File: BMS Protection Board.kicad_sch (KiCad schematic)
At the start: 0 parts

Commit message: worked on MCU
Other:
- sheet BMS_Read_Voltage renamed BMS Read Voltage
- sheet BMS_Thermistors renamed BMS Thermistors
- removed sheet Battery Management System Controller
- added sheet BMS Read Temperature (BMS Read Temperature.kicad_sch)
- sheet BMS Read Voltage: file BMS_Read_Voltage.kicad_sch -> BMS Read Voltage.kicad_sch
- sheet BMS Read Voltage ports: added PACK_READ_STATS; removed PACK_READ_TMP
- sheet BMS Thermistors: file BMS_Thermistors.kicad_sch -> BMS Thermistors.kicad_sch
- sheet Pack Switching and Current Sensing ports: added BATT+, BATT-; removed SCREW_BATT+, SCREW_BATT-

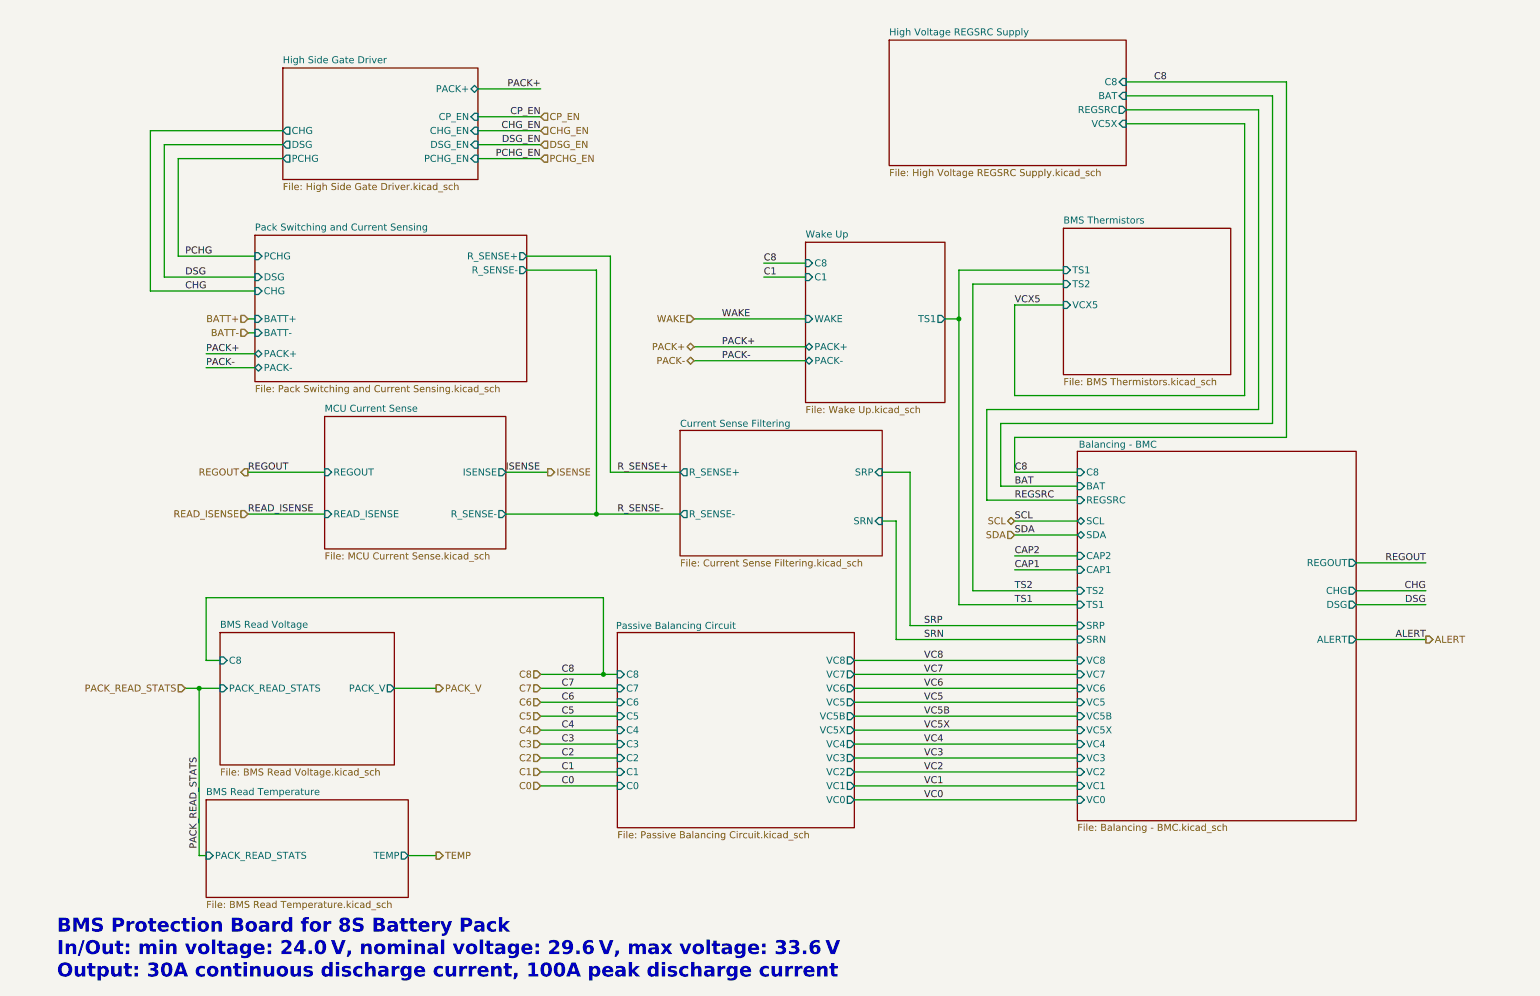
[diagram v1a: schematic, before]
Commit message: commit before simplifying and removing features
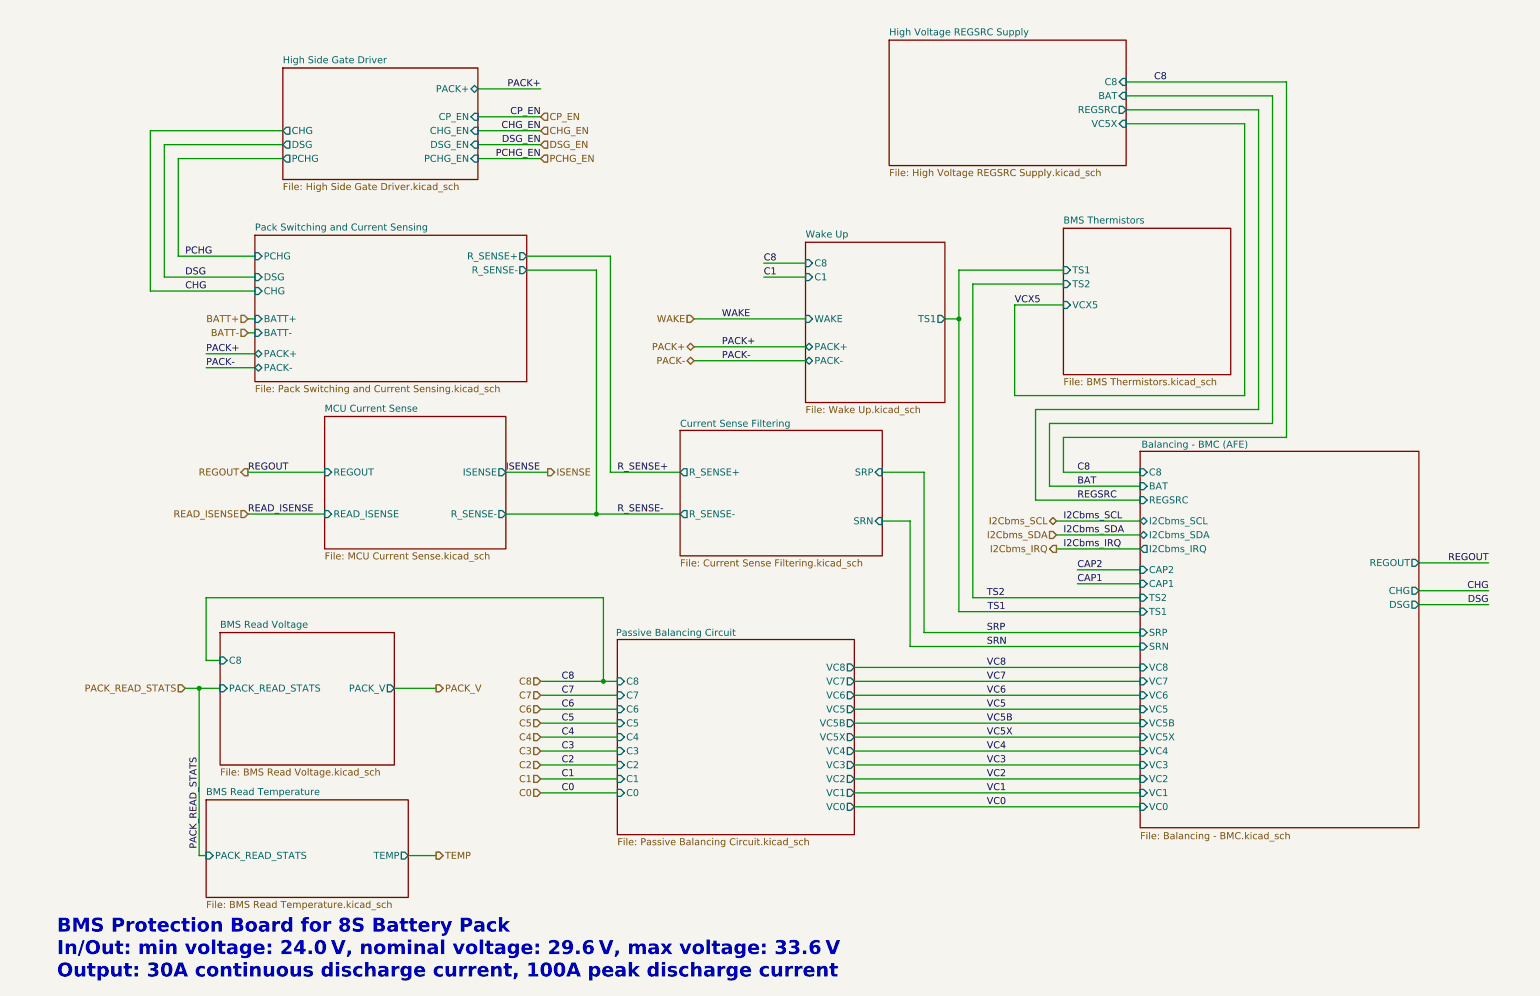
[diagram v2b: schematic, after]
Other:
- sheet Balancing - BMC renamed Balancing - BMC (AFE)
- sheet Balancing - BMC (AFE) ports: added I2Cbms_IRQ, I2Cbms_SCL, I2Cbms_SDA; removed ALERT, SCL, SDA

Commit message: Added Fuel/Gas Guage
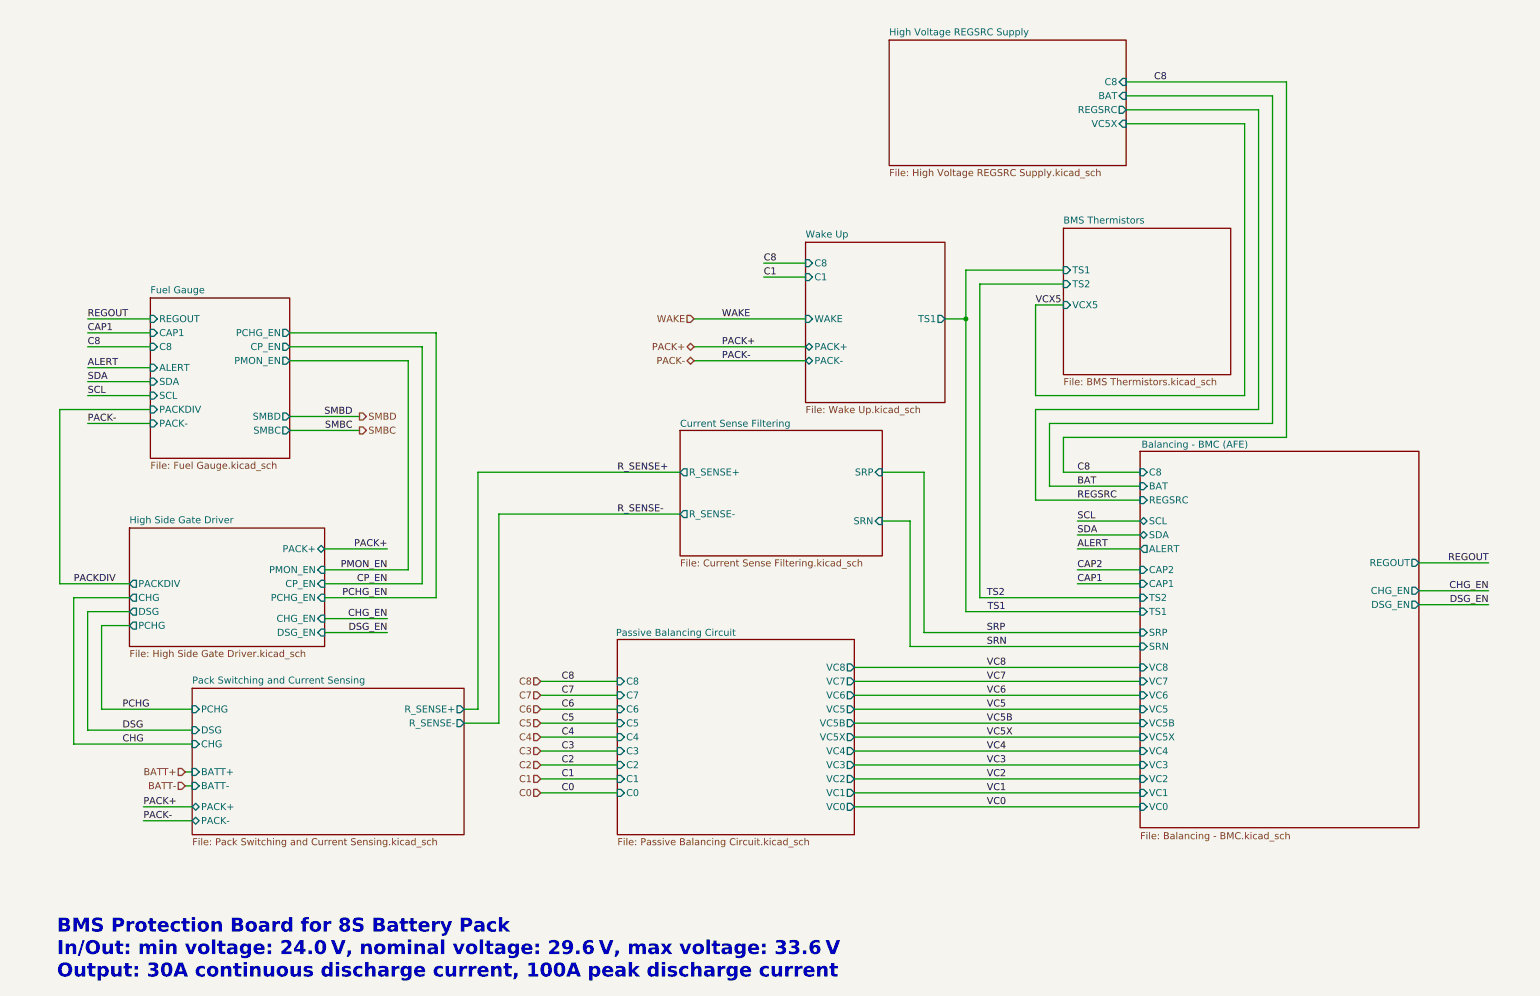
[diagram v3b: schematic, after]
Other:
- removed sheet BMS Read Temperature
- removed sheet BMS Read Voltage
- removed sheet MCU Current Sense
- added sheet Fuel Gauge (Fuel Gauge.kicad_sch)
- sheet Balancing - BMC (AFE) ports: added ALERT, CHG_EN, DSG_EN, SCL, SDA; removed CHG, DSG, I2Cbms_IRQ, I2Cbms_SCL, I2Cbms_SDA
- sheet High Side Gate Driver ports: added PACKDIV, PMON_EN; removed none

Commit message: ready to start first pass review on bms
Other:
- sheet Wake Up ports: added REGOUT; removed C1, PACK-, WAKE
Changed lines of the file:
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@@
-	(wire
-		(pts
-			(xy 138.43 69.85) (xy 158.75 69.85)
-		)
-		(stroke
-			(width 0)
-			(type default)
-		)
-	)
 	(wire
 		(pts
@@
 	(wire
 		(pts
-			(xy 138.43 77.47) (xy 158.75 77.47)
-		)
-		(stroke
-			(width 0)
-			(type default)
-		)
-	)
-	(wire
-		(pts
 			(xy 25.4 120.65) (xy 35.56 120.65)
 		)
@@
 	(wire
 		(pts
-			(xy 151.13 62.23) (xy 158.75 62.23)
+			(xy 158.75 71.12) (xy 146.05 71.12)
 		)
 		(stroke
@@
 	(wire
 		(pts
-			(xy 22.86 118.11) (xy 22.86 86.36)
+			(xy 16.51 118.11) (xy 16.51 86.36)
 		)
 		(stroke
@@
 	(wire
 		(pts
-			(xy 22.86 86.36) (xy 39.37 86.36)
+			(xy 16.51 86.36) (xy 39.37 86.36)
 		)
 		(stroke
@@
 	(wire
 		(pts
-			(xy 22.86 118.11) (xy 35.56 118.11)
+			(xy 16.51 118.11) (xy 35.56 118.11)
 		)
 		(stroke
@@
 		)
 	)
-	(label "WAKE"
-		(at 143.51 69.85 0)
-		(effects
-			(font
-				(size 1.27 1.27)
-			)
-			(justify left bottom)
-		)
-	)
 	(label "DSG_EN"
 		(at 283.21 121.92 180)
@@
 		)
 	)
-	(label "PACK-"
-		(at 143.51 77.47 0)
-		(effects
-			(font
-				(size 1.27 1.27)
-			)
-			(justify left bottom)
-		)
-	)
 	(label "C4"
 		(at 114.3 146.05 0)
@@
 		)
 	)
+	(label "REGOUT"
+		(at 146.05 71.12 0)
+		(effects
+			(font
+				(size 1.27 1.27)
+			)
+			(justify left bottom)
+		)
+	)
 	(label "VC0"
 		(at 191.77 158.75 0)
@@
 	(label "VCX5"
 		(at 200.66 67.31 0)
-		(effects
-			(font
-				(size 1.27 1.27)
-			)
-			(justify left bottom)
-		)
-	)
-	(label "C1"
-		(at 151.13 62.23 0)
 		(effects
 			(font
@@
 		)
 	)
-	(hierarchical_label "PACK-"
-		(shape bidirectional)
-		(at 138.43 77.47 180)
-		(effects
-			(font
-				(size 1.27 1.27)
-			)
-			(justify right)
-		)
-	)
 	(hierarchical_label "C4"
 		(shape input)
@@
 		)
 	)
-	(hierarchical_label "WAKE"
+	(hierarchical_label "PACK-"
 		(shape input)
-		(at 138.43 69.85 180)
+		(at 27.94 88.9 180)
 		(effects
 			(font
@@
 			)
 		)
-		(pin "WAKE" input
-			(at 158.75 69.85 180)
-			(effects
-				(font
-					(size 1.27 1.27)
-				)
-				(justify left)
-			)
-		)
-		(pin "C1" input
-			(at 158.75 62.23 180)
-			(effects
-				(font
-					(size 1.27 1.27)
-				)
-				(justify left)
-			)
-		)
-		(pin "PACK+" bidirectional
-			(at 158.75 74.93 180)
-			(effects
-				(font
-					(size 1.27 1.27)
-				)
-				(justify left)
-			)
-		)
-		(pin "PACK-" bidirectional
-			(at 158.75 77.47 180)
-			(effects
-				(font
-					(size 1.27 1.27)
-				)
-				(justify left)
-			)
-		)
 		(pin "TS1" output
 			(at 184.15 69.85 0)
@@
 			)
 		)
+		(pin "PACK+" input
+			(at 158.75 74.93 180)
+			(effects
+				(font
+					(size 1.27 1.27)
+				)
+				(justify left)
+			)
+		)
+		(pin "REGOUT" input
+			(at 158.75 71.12 180)
+			(effects
+				(font
+					(size 1.27 1.27)
+				)
+				(justify left)
+			)
+		)

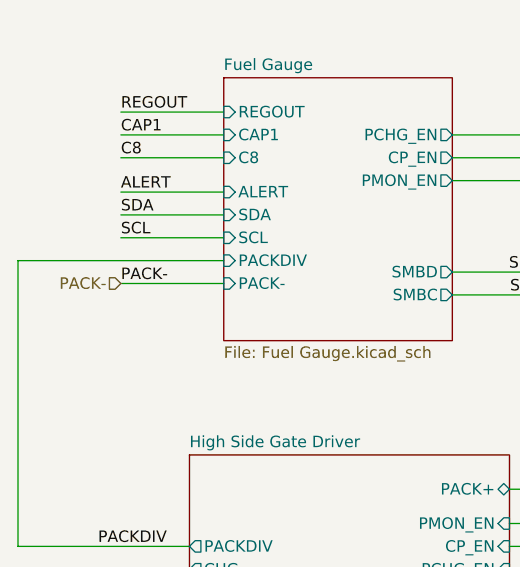
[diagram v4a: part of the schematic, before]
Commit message: I still need to add the 6V line and test points
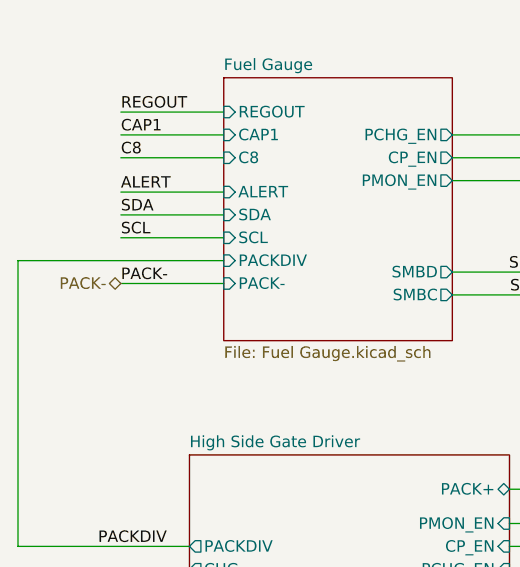
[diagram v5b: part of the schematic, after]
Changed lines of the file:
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@@
 	)
 	(hierarchical_label "PACK-"
-		(shape input)
+		(shape bidirectional)
 		(at 27.94 88.9 180)
 		(effects
@@
 			(project "Project-Star"
 				(path "/fc8533bc-25dd-4c20-9b4c-ffebebd6739b/e8da5d81-614b-4fe5-84b3-4c351fab7114"
-					(page "10")
+					(page "9")
 				)
 			)
@@
 			(project "Project-Star"
 				(path "/fc8533bc-25dd-4c20-9b4c-ffebebd6739b/e8da5d81-614b-4fe5-84b3-4c351fab7114"
-					(page "12")
+					(page "11")
 				)
 			)
@@
 			(project "Project-Star"
 				(path "/fc8533bc-25dd-4c20-9b4c-ffebebd6739b/e8da5d81-614b-4fe5-84b3-4c351fab7114"
-					(page "11")
-				)
-			)
+					(page "10")
+				)
+			)
